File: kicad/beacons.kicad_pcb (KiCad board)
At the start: 2 copper layers, 110.5 x 101.6 mm, 47 parts, among them J1 USB_C_Receptacle_USB2.0_16P, J2 Conn_01x03, J4 Conn_01x02, U1 ESP32-S3-WROOM-1, U2 PN5321A3HN_C1xx, U3 74HC595, U4 MAX17048G+T10, U5 MCP73831-2-OT

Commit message: Tons of stuff
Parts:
- removed C1, C5: 100nF, Capacitor_SMD:C_0402_1005Metric
- removed C10, C11: NFC_C2, Capacitor_SMD:C_0402_1005Metric
- removed C3, C4: 22pF, Capacitor_SMD:C_0402_1005Metric
- removed C6, C7: 220pF, Capacitor_SMD:C_0402_1005Metric
- removed C8, C9: NFC_C1, Capacitor_SMD:C_0402_1005Metric
- removed L1, L2: 560nH, Inductor_SMD:L_0603_1608Metric
- removed R5: 1k, Resistor_SMD:R_0402_1005Metric
- removed R6: 2.7k, Resistor_SMD:R_0402_1005Metric
- removed R7, R8: NFC_RQ, Resistor_SMD:R_0402_1005Metric
- removed U2: PN5321A3HN_C1xx, Package_DFN_QFN:HVQFN-40-1EP_6x6mm_P0.5mm_EP4.1x4.1mm
- added AE1: Antenna_Loop, footprints:NFC, F.Cu at (168.9, 59.7)
- added C15: 47uF, Capacitor_SMD:C_0402_1005Metric, F.Cu at (57.9, 72.7)
- added C16: 10nF, Capacitor_SMD:C_0402_1005Metric, F.Cu at (57.9, 74.7)
- added C17: 47uF, Capacitor_SMD:C_0402_1005Metric, F.Cu at (57.9, 76.6)
- added C19: 47uF, Capacitor_SMD:C_0402_1005Metric, F.Cu at (57.9, 78.6)
- added C21: 47uF, Capacitor_SMD:C_0402_1005Metric, F.Cu at (57.9, 80.6)
- added C22: 10nF, Capacitor_SMD:C_0402_1005Metric, F.Cu at (57.9, 82.5)
- added IC1: AP7179DSKZ20-13, footprints:QFN50P350X350X80-21N-D, F.Cu at (46.7, 75.0)
- added IC2: AP7179DSKZ20-13, footprints:QFN50P350X350X80-21N-D, F.Cu at (46.7, 80.8)
- added IC3: PN7160A1HN_C100E, footprints:QFN50P600X600X100-41N-D, F.Cu at (83.6, 83.4)
- added R11: 10k, Resistor_SMD:R_0402_1005Metric, F.Cu at (60.8, 79.3)
- added SW2: SW_SPST, Connector_JST:JST_PH_B2B-PH-K_1x02_P2.00mm_Vertical, F.Cu at (62.4, 74.4)
- moved J2 26.3 mm to (179.8, 113.6)
- moved J4 2.64 mm to (179.1, 129.5)
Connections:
- net LED_SPI renamed LED_SPI_5V
- U4 pad 6: I2C_SCL -> unconnected-(U4-QSTRT-Pad6)
- U4 pad 8: I2C_SCL -> I2C_SDA
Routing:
- net Net-(AE1-Pad2): track 0.00 -> 3.51 mm
- net Net-(AE1-Pad1): track 0.00 -> 1.01 mm
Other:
- board size 110.5 x 101.6 mm -> 118.1 x 101.6 mm

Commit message: Routing and RF
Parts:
- removed D10, D11: WS2812B, LED_SMD:LED_WS2812B_PLCC4_5.0x5.0mm_P3.2mm
- added C1: 100nF, Capacitor_SMD:C_0402_1005Metric, B.Cu at (217.4, 71.2)
- added C10: 100nF, Capacitor_SMD:C_0402_1005Metric, B.Cu at (226.8, 67.4)
- added C11: 4.7uF, Capacitor_SMD:C_0402_1005Metric, B.Cu at (219.3, 75.2)
- added C18: 10nF, Capacitor_SMD:C_0402_1005Metric, B.Cu at (148.2, 72.3)
- added C20: 10nF, Capacitor_SMD:C_0402_1005Metric, B.Cu at (150.9, 79.3)
- added C23: C_RX, Capacitor_SMD:C_0402_1005Metric, B.Cu at (216.3, 72.3)
- added C24: C_RX, Capacitor_SMD:C_0402_1005Metric, B.Cu at (219.3, 68.6)
- added C25: C_0, Capacitor_SMD:C_0402_1005Metric, B.Cu at (212.0, 69.9)
- added C26: C_ANT, Capacitor_SMD:C_0402_1005Metric, B.Cu at (210.7, 66.5)
- added C27: C_0, Capacitor_SMD:C_0402_1005Metric, B.Cu at (213.9, 69.9)
- added C29: C_1, Capacitor_SMD:C_0402_1005Metric, B.Cu at (210.0, 69.9)
- added C3: 2.2uF, Capacitor_SMD:C_0402_1005Metric, B.Cu at (218.2, 75.2)
- added C31: C_1, Capacitor_SMD:C_0402_1005Metric, B.Cu at (212.6, 68.8)
- added C33: C_2, Capacitor_SMD:C_0402_1005Metric, B.Cu at (208.5, 69.2)
- added C34: C_2, Capacitor_SMD:C_0402_1005Metric, B.Cu at (212.8, 67.6)
- added C4: 2.2uF, Capacitor_SMD:C_0402_1005Metric, B.Cu at (229.4, 72.6)
- added C5: 22pF, Capacitor_SMD:C_0402_1005Metric, B.Cu at (232.1, 68.9)
- added C6: 22pF, Capacitor_SMD:C_0402_1005Metric, B.Cu at (228.8, 66.6)
- added C7: 2.2uF, Capacitor_SMD:C_0402_1005Metric, B.Cu at (222.9, 67.2)
- added C8: 2.2uF, Capacitor_SMD:C_0402_1005Metric, B.Cu at (229.4, 71.5)
- added C9: 4.7uF, Capacitor_SMD:C_0402_1005Metric, B.Cu at (225.0, 67.3)
- added J5: Conn_01x06, Connector_JST:JST_PH_B6B-PH-K_1x06_P2.00mm_Vertical, B.Cu at (228.2, 80.0)
- added J6: Conn_01x06, Connector_JST:JST_PH_B6B-PH-K_1x06_P2.00mm_Vertical, B.Cu at (161.0, 46.8)
- added L1: L_0, Inductor_SMD:L_0402_1005Metric, B.Cu at (211.6, 71.4)
- added L2: L_0, Inductor_SMD:L_0402_1005Metric, B.Cu at (215.9, 69.9)
- added Q1: Q_NPN, Package_TO_SOT_SMD:SOT-23, B.Cu at (85.1, 130.8)
- added R12: 12.4k, Resistor_SMD:R_0402_1005Metric, B.Cu at (146.5, 73.8)
- added R13: 2.37k, Resistor_SMD:R_0402_1005Metric, B.Cu at (150.5, 72.3)
- added R14: 11.8k, Resistor_SMD:R_0402_1005Metric, B.Cu at (148.9, 79.3)
- added R15: 3.74k, Resistor_SMD:R_0402_1005Metric, B.Cu at (147.0, 81.2)
- added R16: R_ANT, Resistor_SMD:R_0402_1005Metric, B.Cu at (208.5, 67.2)
- added R5: R_RX, Resistor_SMD:R_0402_1005Metric, B.Cu at (214.3, 72.3)
- added R6: R_RX, Resistor_SMD:R_0402_1005Metric, B.Cu at (217.3, 68.6)
- added R7: R_Q, Resistor_SMD:R_0402_1005Metric, B.Cu at (210.1, 67.6)
- added R8: R_Q, Resistor_SMD:R_0402_1005Metric, B.Cu at (213.0, 66.5)
- added Y1: 27.12MHz Crystal, Crystal:Crystal_SMD_2016-4Pin_2.0x1.6mm, B.Cu at (229.5, 68.4)
- C12, C13, C14, C15, C16, C17, C19, C2, C21, C22, D1, IC1, IC2, IC3, R1, R10, R11, R2, R3, R4, R9: moved to B.Cu
- J4: footprint Connector_JST:JST_PH_B2B-PH-K_1x02_P2.00mm_Vertical -> Connector_AMASS:AMASS_XT30UPB-M_1x02_P5.0mm_Vertical
- SW2: footprint Connector_JST:JST_PH_B2B-PH-K_1x02_P2.00mm_Vertical -> Connector_AMASS:AMASS_XT30UPB-M_1x02_P5.0mm_Vertical; moved to B.Cu
- moved IC3 141.1 mm to (224.2, 72.3), turned to 90 degrees
- moved D1 112.0 mm to (144.3, 98.0), turned to 180 degrees
- moved IC1 103.3 mm to (150.0, 75.6)
- moved IC2 103.3 mm to (150.0, 82.5)
- moved C21 99.2 mm to (156.9, 87.8), turned to 90 degrees
- moved C15 99.0 mm to (156.9, 74.4), turned to -90 degrees
- moved SW2 98.8 mm to (161.1, 76.8), turned to -90 degrees
- moved C12 98.4 mm to (153.7, 94.0)
- moved C22 96.5 mm to (154.4, 81.1), turned to -90 degrees
- moved C16 96.5 mm to (154.4, 74.4), turned to -90 degrees
- moved C13 96.0 mm to (153.2, 90.7), turned to -90 degrees
- moved C14 92.5 mm to (148.0, 96.2), turned to -90 degrees
- moved R10 92.1 mm to (145.7, 93.7), turned to -90 degrees
- moved C17 88.0 mm to (145.9, 77.6), turned to 90 degrees
- moved C19 87.1 mm to (145.0, 81.0), turned to -90 degrees
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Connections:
- net CELL_POS renamed /CELL_POS
- net CHARGE_STAT renamed /CHARGE_STAT
- net ESP_BOOT renamed /ESP_BOOT
- net LED_SPI renamed /LED_SPI
- net REG_POS renamed /REG_POS
- net SPI_CLK renamed /SPI_CLK
- net SPI_DATA0 renamed /SPI_DATA0
- net SR_CS renamed /SR_CS
- net SS0 renamed /SS0
- net SS1 renamed /SS1
- net USB_NEG renamed /USB_NEG
- net USB_POS renamed /USB_POS
- C14 pad 2: USB_VBUS -> /USB_VBUS
- C17 pad 2: USB_VBUS -> +5V
- D1 pad 1: USB_VBUS -> /USB_VBUS
- D2 pad 1: USB_VBUS -> +5V
- D2 pad 4: LED_SPI_5V -> /LED_SPI_5V
- D3 pad 1: USB_VBUS -> +5V
- D4 pad 1: USB_VBUS -> +5V
- D5 pad 1: USB_VBUS -> +5V
- D6 pad 1: USB_VBUS -> +5V
- D7 pad 1: USB_VBUS -> +5V
- D8 pad 1: USB_VBUS -> +5V
- D9 pad 1: USB_VBUS -> +5V
- D9 pad 2: Net-(D10-DIN) -> /LED_PEAK
- IC1 pad 1: USB_VBUS -> +5V
- IC3 pad 1: GND -> /NFC/NFC_GND
- IC3 pad 10: +3V3 -> /NFC/NFC_3V3
- IC3 pad 12: Net-(IC3-VBAT) -> /NFC/NFC_3V3
- IC3 pad 13: Net-(IC3-VDD(UP)) -> /NFC/NFC_3V3
- IC3 pad 14: Net-(IC3-TVDD_IN) -> /NFC/NFC_3V3
- IC3 pad 15: NFC_RXN -> /NFC/NFC_RXN
- IC3 pad 16: NFC_RXP -> /NFC/NFC_RXP
- IC3 pad 18: Net-(IC3-TVDD_IN) -> /NFC/NFC_3V3
- IC3 pad 19: NFC_TX2 -> /NFC/NFC_TX2
- IC3 pad 2: NFC_FWUD -> /NFC/NFC_FWUD
- IC3 pad 20: GND -> unconnected-(IC3-VSS(TX)-Pad20)
- IC3 pad 21: NFC_TX1 -> /NFC/NFC_TX1
- IC3 pad 22: Net-(IC3-TVDD_IN) -> /NFC/NFC_3V3
- IC3 pad 26: Net-(IC3-VDD(A)) -> /NFC/NFC_3V3
- IC3 pad 27: Net-(IC3-VDD(A)) -> /NFC/NFC_3V3
- IC3 pad 3: GND -> /NFC/NFC_GND
- IC3 pad 31: Net-(IC3-VDD(A)) -> /NFC/NFC_3V3
- IC3 pad 4: GND -> /NFC/NFC_GND
- IC3 pad 41: GND -> /NFC/NFC_GND
- IC3 pad 5: I2C_SDA -> /NFC/I2C_SDA
- IC3 pad 6: Net-(IC3-VDD(A)) -> /NFC/NFC_3V3
- IC3 pad 7: I2C_SCL -> /NFC/I2C_SCL
- IC3 pad 8: NFC_IRQ -> /NFC/NFC_IRQ
- IC3 pad 9: GND -> /NFC/NFC_GND
- J2 pad 2: LED_PEAK -> /LED_PEAK
- J2 pad 3: USB_VBUS -> +5V
- LED1 pad 14: unconnected-(LED1-Pad14) -> Net-(LED1-Pad14)
- LED1 pad 3: unconnected-(LED1-Pad3) -> Net-(LED1-Pad14)
- LED1 pad 6: Net-(LED1-Pad6) -> Net-(LED1-Pad14)
- LED2 pad 14: unconnected-(LED2-Pad14) -> Net-(LED2-Pad14)
- LED2 pad 3: unconnected-(LED2-Pad3) -> Net-(LED2-Pad14)
- LED2 pad 6: Net-(LED2-Pad6) -> Net-(LED2-Pad14)
- R1 pad 1: Net-(LED1-Pad6) -> Net-(LED1-Pad14)
- R2 pad 1: Net-(LED2-Pad6) -> Net-(LED2-Pad14)
- U3 pad 10: VCC -> +3V3
- U4 pad 6: unconnected-(U4-QSTRT-Pad6) -> GND
- U4 pad 7: I2C_SCL -> /I2C_SCL
- U4 pad 8: I2C_SDA -> /I2C_SDA
- U5 pad 4: USB_VBUS -> /USB_VBUS
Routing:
- net +5V: track 0.00 -> 177.8 mm, vias 0 -> 2
- net +3V3: track 0.00 -> 130.9 mm, vias 0 -> 2
- net Net-(D1-A): track 0.00 -> 123.3 mm
- net /LED_PEAK: track 0.00 -> 81.8 mm
- net /NFC/NFC_3V3: track 0.00 -> 63.9 mm, vias 0 -> 4
- net /S6: track 0.00 -> 46.1 mm
- net /S5: track 0.00 -> 46.0 mm
- net /S1: track 0.00 -> 42.9 mm
- net /S0: track 0.00 -> 42.4 mm
- net /CELL_POS: track 0.00 -> 41.8 mm
- net /S7: track 0.00 -> 37.5 mm
- net /S3: track 0.00 -> 33.8 mm
- net /S4: track 0.00 -> 32.9 mm, vias 0 -> 1
- net /S2: track 0.00 -> 31.0 mm
- net Net-(LED2-Pad14): track 0.00 -> 27.2 mm
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- added copper zone on B.Cu, net /NFC/NFC_GND
- added copper zone on F.Cu, net /NFC/NFC_GND
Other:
- board size 118.1 x 101.6 mm -> 170.2 x 119.6 mm

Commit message: First revision
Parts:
- added C28: .1uF, Capacitor_SMD:C_0402_1005Metric, B.Cu at (77.2, 83.1)
- added C30: .1uF, Capacitor_SMD:C_0402_1005Metric, B.Cu at (86.5, 86.9)
- added C32: 22uF, Capacitor_SMD:C_0402_1005Metric, B.Cu at (82.1, 93.0)
- added J3: Conn_01x18, footprints:DisplayConnector, B.Cu at (160.7, 105.5)
- added SW1: SW_Push, footprints:SMT_4.2X3.2_, B.Cu at (82.3, 79.2)
- added SW2: SW_Push, footprints:SMT_4.2X3.2_, B.Cu at (82.3, 85.8)
- moved C25 38.1 mm to (193.1, 103.0)
- moved C27 38.1 mm to (195.0, 103.0)
- moved C34 38.1 mm to (193.8, 100.7)
- moved C5 38.1 mm to (213.2, 102.0)
- moved C8 38.1 mm to (210.5, 104.6)
- moved L2 38.1 mm to (197.0, 103.0)
- moved R7 38.1 mm to (191.1, 100.7)
- moved Y1 38.1 mm to (210.6, 101.5)
- moved AE1 38.1 mm to (204.6, 83.6)
- moved C1 38.1 mm to (198.5, 104.3)
- moved C10 38.1 mm to (207.9, 100.5)
- moved C11 38.1 mm to (200.4, 108.3)
- moved C23 38.1 mm to (197.4, 105.4)
- moved C24 38.1 mm to (200.4, 101.7)
- moved C26 38.1 mm to (191.8, 99.6)
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- renumbered SW2 to SW3
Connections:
- IC3 pad 20: unconnected-(IC3-VSS(TX)-Pad20) -> /NFC/NFC_GND
- R9 pad 1: /ESP_BOOT -> +3V3
- R9 pad 2: +3V3 -> /ESP_EN
- U1 pad 10: unconnected-(U1-GPIO17/U1TXD/ADC2_CH6-Pad10) -> /SS1
- U1 pad 11: unconnected-(U1-GPIO18/U1RXD/ADC2_CH7/CLK_OUT3-Pad11) -> /NFC_IRQ
- U1 pad 12: unconnected-(U1-GPIO8/TOUCH8/ADC1_CH7/SUBSPICS1-Pad12) -> /CHARGE_STAT
- U1 pad 15: unconnected-(U1-GPIO3/TOUCH3/ADC1_CH2-Pad15) -> /NFC_FWUD
- U1 pad 17: unconnected-(U1-GPIO9/TOUCH9/ADC1_CH8/FSPIHD/SUBSPIHD-Pad17) -> /TOUCH_IRQ
- U1 pad 18: unconnected-(U1-GPIO10/TOUCH10/ADC1_CH9/FSPICS0/FSPIIO4/SUBSPICS0-Pad18) -> /I2C_SDA
- U1 pad 19: unconnected-(U1-GPIO11/TOUCH11/ADC2_CH0/FSPID/FSPIIO5/SUBSPID-Pad19) -> /I2C_SCL
- U1 pad 20: unconnected-(U1-GPIO12/TOUCH12/ADC2_CH1/FSPICLK/FSPIIO6/SUBSPICLK-Pad20) -> /TOUCH_RESET
- U1 pad 21: unconnected-(U1-GPIO13/TOUCH13/ADC2_CH2/FSPIQ/FSPIIO7/SUBSPIQ-Pad21) -> /DISP_RESET
- U1 pad 22: unconnected-(U1-GPIO14/TOUCH14/ADC2_CH3/FSPIWP/FSPIDQS/SUBSPIWP-Pad22) -> /SPI_DATA3
- U1 pad 23: unconnected-(U1-GPIO21-Pad23) -> /SPI_DATA2
- U1 pad 24: unconnected-(U1-GPIO47/SPICLK_P/SUBSPICLK_P_DIFF-Pad24) -> /SPI_DATA1
- U1 pad 25: unconnected-(U1-GPIO48/SPICLK_N/SUBSPICLK_N_DIFF-Pad25) -> /SPI_DATA0
- U1 pad 26: unconnected-(U1-GPIO45-Pad26) -> /SPI_CLK
- U1 pad 3: +3V3 -> /ESP_EN
- U1 pad 36: unconnected-(U1-U0RXD/GPIO44/CLK_OUT2-Pad36) -> /DISP_CS
- U1 pad 37: unconnected-(U1-U0TXD/GPIO43/CLK_OUT1-Pad37) -> /LED_SPI
- U1 pad 4: unconnected-(U1-GPIO4/TOUCH4/ADC1_CH3-Pad4) -> /SR_CS
- U1 pad 9: unconnected-(U1-GPIO16/U0CTS/ADC2_CH5/XTAL_32K_N-Pad9) -> /SS0
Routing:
- net /I2C_SCL: track 0.00 -> 156.3 mm, vias 0 -> 1
- net /I2C_SDA: track 0.00 -> 145.2 mm, vias 0 -> 1
- net /SPI_DATA0: track 0.00 -> 118.0 mm, vias 0 -> 2
- net /SPI_CLK: track 0.00 -> 115.6 mm, vias 0 -> 2
- net /NFC_IRQ: track 0.00 -> 104.7 mm, vias 0 -> 1
- net /NFC_FWUD: track 0.00 -> 96.8 mm, vias 0 -> 1
- net /DISP_CS: track 0.00 -> 78.6 mm
- net +3V3: track 130.9 -> 208.8 mm
- net /TOUCH_IRQ: track 0.00 -> 65.6 mm, vias 0 -> 1
- net /TOUCH_RESET: track 0.00 -> 65.6 mm
- net /DISP_RESET: track 0.00 -> 65.6 mm
- net /SPI_DATA3: track 0.00 -> 65.6 mm
- net /SPI_DATA2: track 0.00 -> 65.6 mm
- net /SPI_DATA1: track 0.00 -> 65.6 mm
- net /CHARGE_STAT: track 0.00 -> 61.3 mm, vias 0 -> 2
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- added copper zone on B.Cu, net GND
- added copper zone on F.Cu, net GND
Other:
- board size 170.2 x 119.6 mm -> 151.3 x 106.7 mm
- board text added: "BOOT"
- board text added: "Designed by Jack Hogan"
- board text added: "Purdue Hackers Beacons Mainboard Rev 1.0 Designed by Jack Hogan"
- board text added: "Purdue Hackers Beacons NFC Board Rev 1.0"
- board text added: "RESET"

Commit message: Added level shifter
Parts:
- removed Q1: Q_NPN, Package_TO_SOT_SMD:SOT-23
- removed the R11 at (86.1, 126.4)
- added U2: SN74LVC1T45DCK, Package_TO_SOT_SMD:SOT-363_SC-70-6, B.Cu at (85.9, 129.9)
- renumbered R16 to R11
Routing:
- net +3V3: track 208.8 -> 276.4 mm, vias 2 -> 4
- net /LED_SPI: track 15.5 -> 20.1 mm
- net Net-(Q1-B): track 2.96 -> 0.00 mm
- net +5V: track 181.8 -> 183.8 mm
- net /LED_SPI_5V: track 5.93 -> 7.51 mm
- net GND: vias 5 -> 6

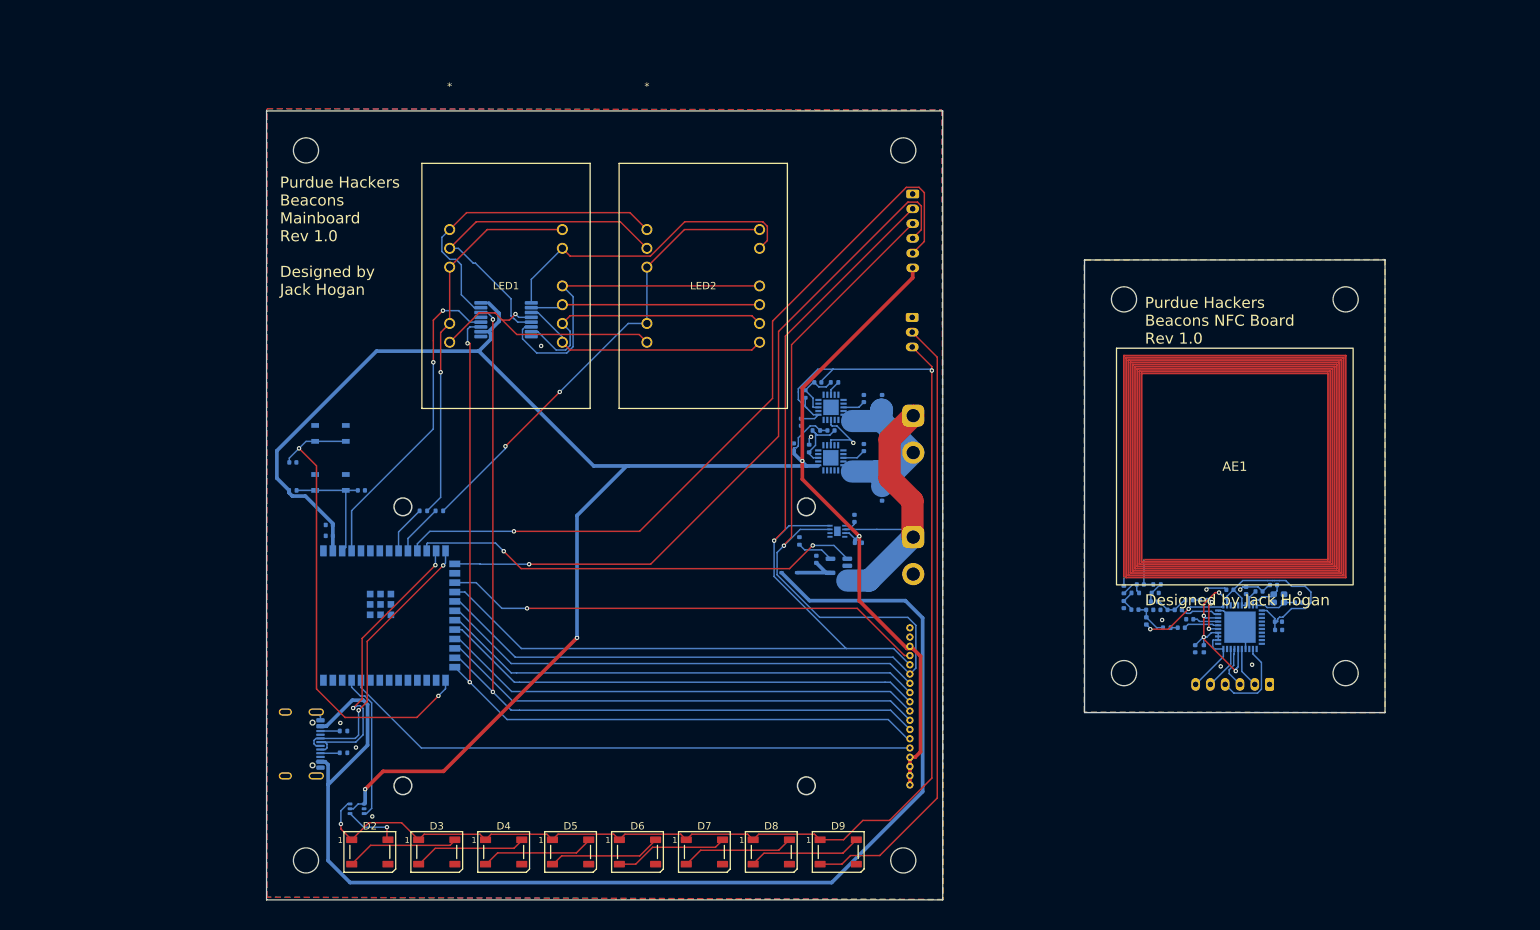
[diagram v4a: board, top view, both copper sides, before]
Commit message: Added NFC enable pin
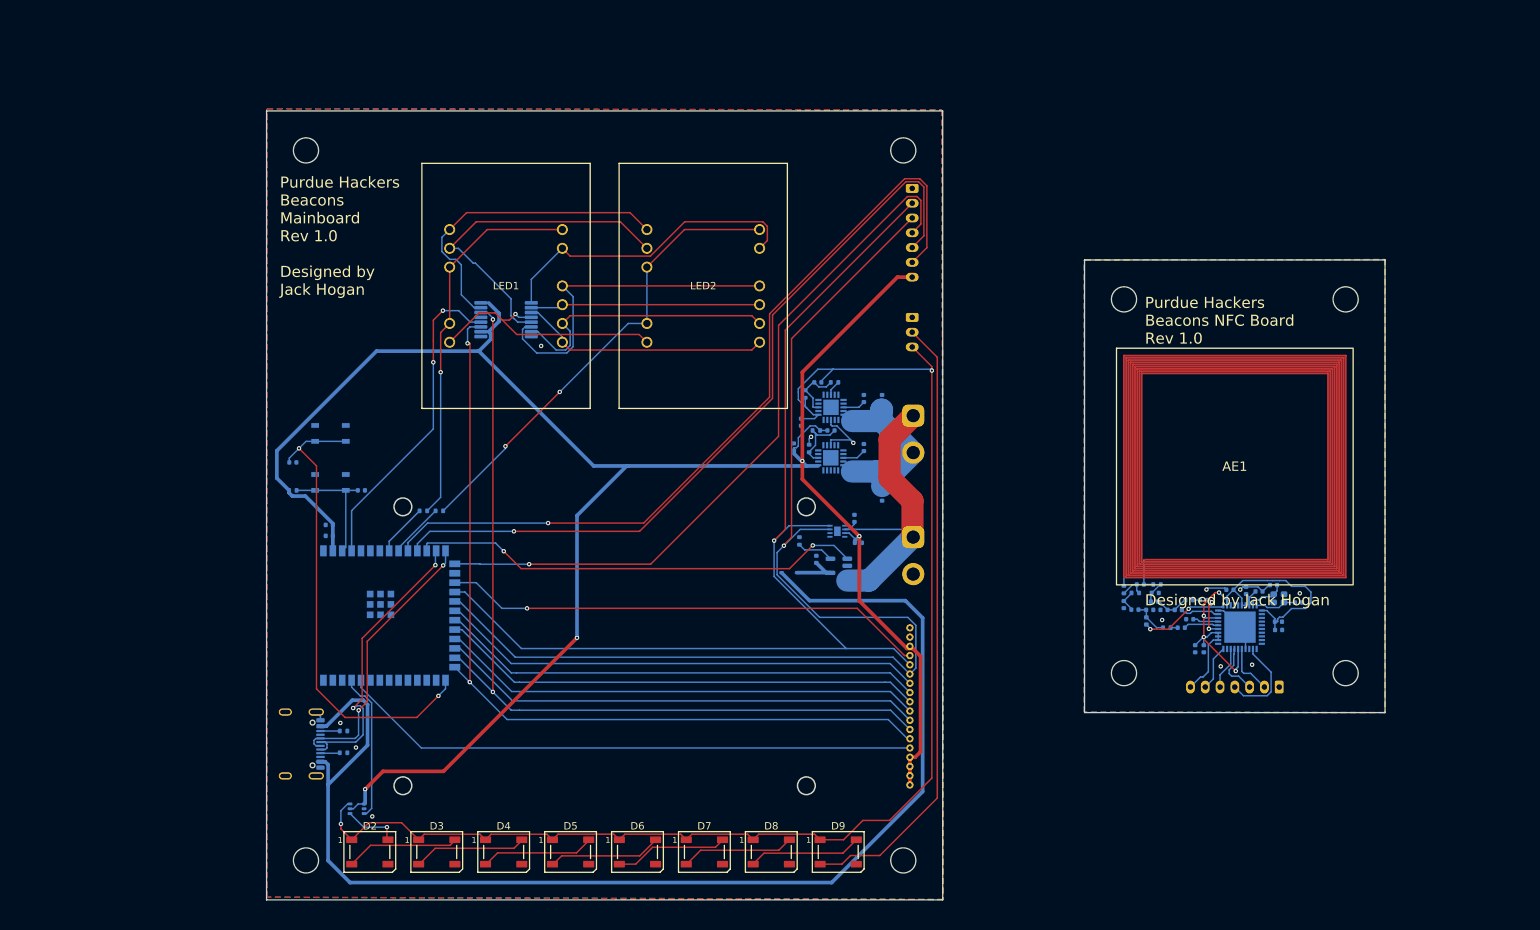
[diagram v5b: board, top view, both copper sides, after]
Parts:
- J5, J6: value Conn_01x06 -> Conn_01x07; footprint Connector_JST:JST_PH_B6B-PH-K_1x06_P2.00mm_Vertical -> Connector_JST:JST_PH_B7B-PH-K_1x07_P2.00mm_Vertical
- moved J5 1.35 mm to (210.6, 113.5)
- moved J6 0.76 mm to (161.0, 46.0)
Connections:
- IC3 pad 10: /NFC/NFC_3V3 -> /NFC/NFC_EN
- J5 pad 6: /NFC/NFC_3V3 -> /NFC/NFC_EN
- J6 pad 6: +3V3 -> /NFC_EN
- U1 pad 10: /SS1 -> /NFC_EN
- U1 pad 8: unconnected-(U1-GPIO15/U0RTS/ADC2_CH4/XTAL_32K_P-Pad8) -> /SS0
- U1 pad 9: /SS0 -> /SS1
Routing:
- net /NFC_EN: track 0.00 -> 109.8 mm, vias 0 -> 1
- net /NFC/NFC_EN: track 0.00 -> 6.16 mm
- net /NFC/I2C_SCL: track 5.72 -> 7.17 mm
- net /NFC/I2C_SDA: track 5.52 -> 6.97 mm
- net /NFC/NFC_3V3: track 64.9 -> 63.5 mm
- net /NFC/NFC_FWUD: track 11.5 -> 12.4 mm
- net /NFC_IRQ: track 104.7 -> 105.5 mm
- net /NFC_FWUD: track 96.8 -> 97.5 mm
- net /I2C_SDA: track 145.2 -> 145.9 mm
- net /I2C_SCL: track 156.3 -> 157.0 mm
- net /SS1: track 6.95 -> 7.48 mm
- net /SS0: track 6.58 -> 7.11 mm
